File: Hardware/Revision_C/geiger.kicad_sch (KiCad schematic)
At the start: 23 parts, among them J1 I2C 5V, J2 I2C 3V3, J3 GND, U3 BSP125

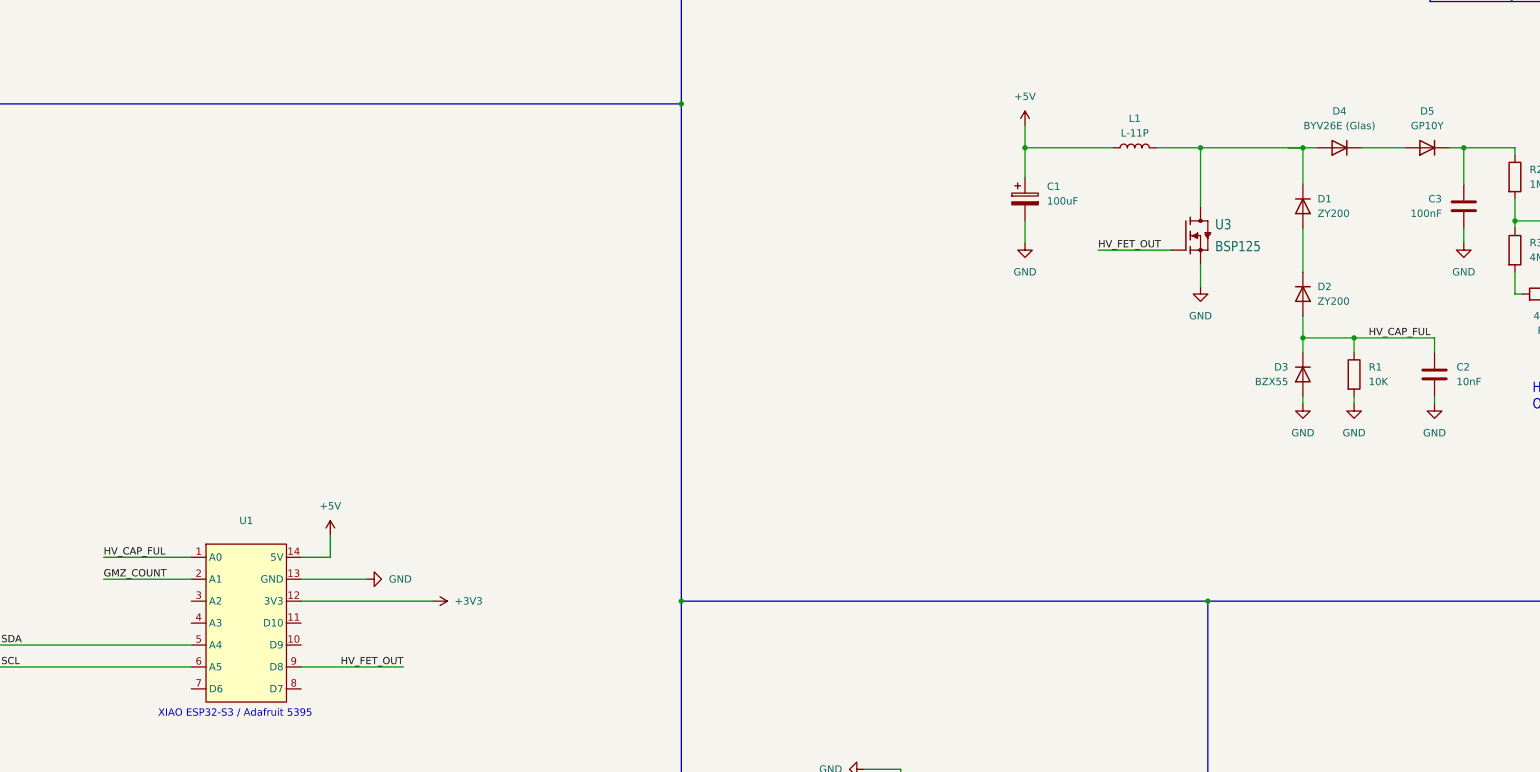
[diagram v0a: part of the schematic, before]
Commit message: Hardware: Rev B V2 + Rev C V2 — layout update to remove HV-to-counter crosstalk
Why these boards were redesigned:

The previous Rev B (Feather form factor) and Rev C (XIAO form factor)
carrier PCBs could register phantom Geiger counts: each pulse of the
high-voltage boost supply coupled a small spike into the tube counting
input. Long-term field data and bench probing traced the root cause to
the layout, not the circuit:

- The module socket pinout placed the counting input (GMZ_COUNT) directly
  beside the HV regulation sense net (HV_CAP_FUL), 2.54 mm pad to pad, so
  the most sensitive high-impedance node on the board (1 Mohm) was forced
  to run alongside its noisiest neighbour before routing even started.
- The counting trace crossed gaps in the ground plane (the worst void sat
  under the unused JP1 header on Rev B), weakening its return path exactly
  where the coupling occurred.

Firmware (V2.6.31+) fully compensates the phantom pulses by blanking, so
deployed nodes read correctly, but these V2 boards remove the coupling at
the source. What changed vs the previous revisions:

- Pin roles swapped at the module socket: GMZ_COUNT <-> HV_FET_OUT. The
  counting input now sits >=10 mm from both HV nets; the FET gate (a
  driven, low-impedance net) takes the seat next to the HV sense line.
- JP1 removed (Rev B), closing the ground-plane slot its through-holes cut.
- Routing rules enforced by DRC: >=2 mm clearance between the counting
  trace and both HV nets; crossings only on the opposite layer at 90 deg.
- Ground rebuilt: solid pours both sides with ~700 stitching vias; ground
  return coverage under the counting trace raised from ~79% to ~87%
  (Rev B; Rev C similar). The previous boards had no stitching vias near
  the counting run.
- Mounting holes enlarged 2.2 -> 2.7 mm to suit M2.5 hardware.
- The HV generation circuit itself is deliberately untouched: same
  schematic, same BOM, same tube chain.

IMPORTANT — FIRMWARE COMPATIBILITY: the pin-role swap makes b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
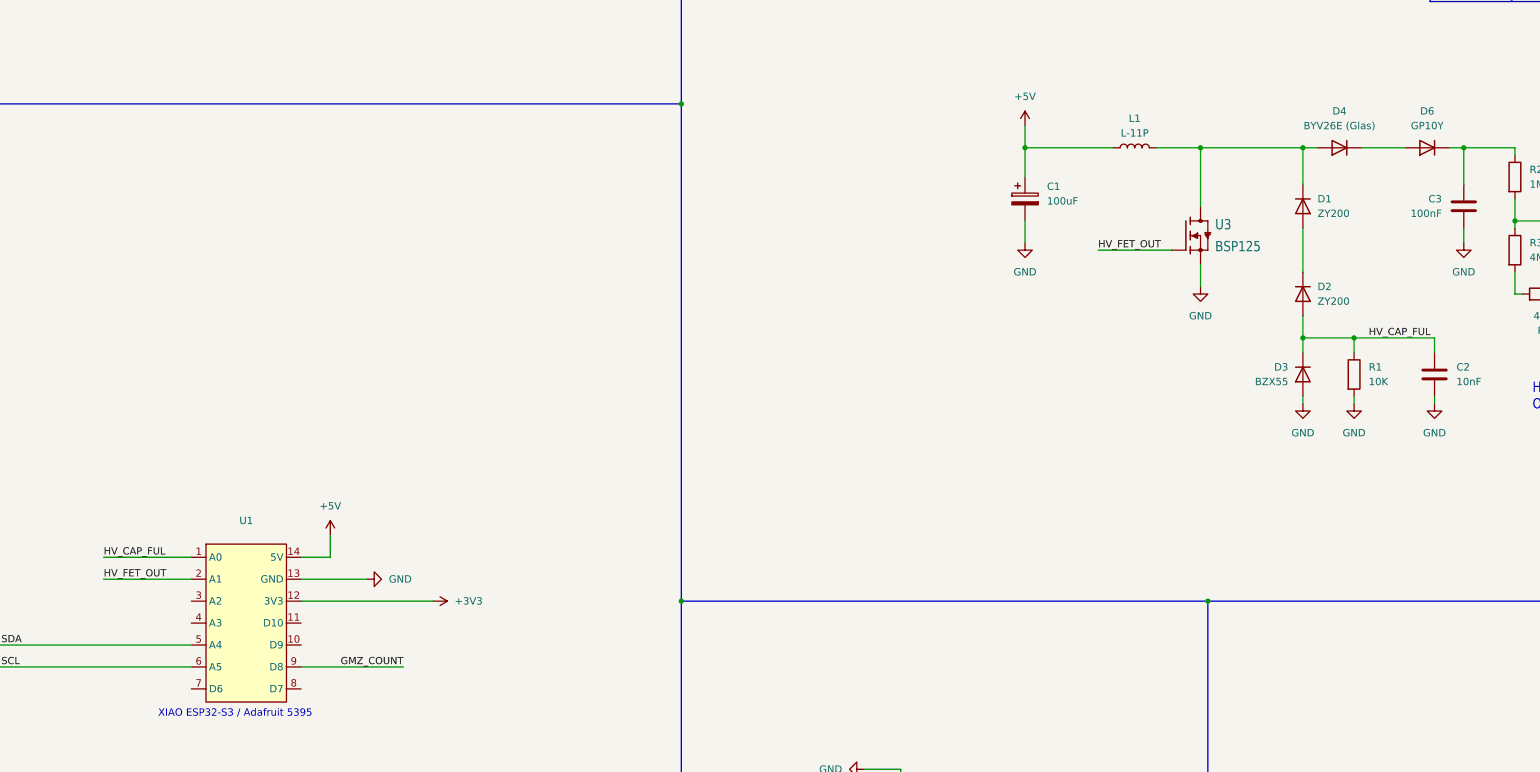
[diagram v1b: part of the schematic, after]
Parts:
- U1: value ~ -> (none)
- renumbered D5 to D6
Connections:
- net GMZ_COUNT: now also U1.9 (D8); no longer U1.2 (A1)
- net HV_FET_OUT: now also U1.2 (A1); no longer U1.9 (D8)

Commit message: Hardware: add manufacturer part numbers to the BOMs and schematics
Rev A: update PARTS in gen_v110_bom_cpl.py and regenerate the BOM.
Rev B and Rev C: add a Part Number field to each schematic symbol and
push it to the PCB footprints.

Part number updates: C3 R75 -> R76, D3 BZX55 -> BZX79-B3V3,
R2-R5 MFR-25 -> RNV14, R6 RNV14FAL100K.

Also fixes the D3 part number CSV quoting, adds the missing tube-clip
and GND test-point rows, corrects the D3 and L1 values, and renames the
Rev C tube holder to SBM-19/20 to match the PCB.

Board geometry is unchanged.
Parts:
- C1: Part Number (none) -> 16SEPC100MW
- C2: Part Number (none) -> MKP2D021001B00KSSD
- C3: Part Number (none) -> R76PI31005050J
- C4: Part Number (none) -> FKP2O101001D00JSSD
- D1, D2: Part Number (none) -> ZY200
- D3: value BZX55 -> BZX79-B3V3; Part Number (none) -> BZX79-B3V3,133
- D4: Part Number (none) -> BYV26E
- D6: Part Number (none) -> GP10Y
- J1: Part Number (none) -> PH-4P
- J2: Part Number (none) -> SM04B-SRSS-TB(LF)(SN)
- L1: value L-11P -> 150mH; Part Number (none) -> 11P-154J-50
- R1, R6, R7: Part Number (none) -> UXB02070F1002AR100
- R2, R5: Part Number (none) -> RNV14FAL1M00
- R3, R4: Part Number (none) -> RNV14FAL4M70
- SBM-19/20: renamed from SBM-19/1; Part Number (none) -> 8040.0003
- U3: Part Number (none) -> BSP125H6327
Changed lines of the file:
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@@
 		(dnp no)
 		(fields_autoplaced yes)
-		(property "Reference" "SBM-19/1"
+		(property "Reference" "SBM-19/20"
 			(at 382.27 95.2499 0)
 			(show_name no)
@@
 			)
 		)
-		(property "Untitled Field" ""
+		(property "Part Number" "8040.0003"
 			(at 383.8474 105.41 0)
 			(hide yes)
@@
 			(project "geiger"
 				(path "/29f38b98-cdf0-4588-b893-03ee7a6e5052"
-					(reference "SBM-19/1")
+					(reference "SBM-19/20")
 					(unit 1)
 				)
@@
 			)
 		)
-		(property "Untitled Field" ""
+		(property "Part Number" "RNV14FAL4M70"
 			(at 325.12 85.09 0)
 			(hide yes)
@@
 			)
 		)
-		(property "Untitled Field" ""
+		(property "Part Number" "16SEPC100MW"
 			(at 240.03 76.2 0)
 			(hide yes)
@@
 			)
 		)
-		(property "Value" "L-11P"
+		(property "Value" "150mH"
 			(at 259.08 64.77 90)
 			(show_name no)
@@
 			)
 		)
+		(property "Part Number" "11P-154J-50"
+			(at 259.08 67.31 90)
+			(hide yes)
+			(show_name no)
+			(do_not_autoplace no)
+			(effects
+				(font
+					(size 1.27 1.27)
+				)
+			)
+		)
 		(pin "2"
 		)
@@
 			)
 		)
-		(property "Untitled Field" ""
+		(property "Part Number" "RNV14FAL1M00"
 			(at 325.12 72.39 0)
 			(hide yes)
@@
 			)
 		)
+		(property "Part Number" "FKP2O101001D00JSSD"
+			(at 335.28 80.01 90)
+			(hide yes)
+			(show_name no)
+			(do_not_autoplace no)
+			(effects
+				(font
+					(size 1.27 1.27)
+				)
+			)
+		)
 		(pin "1"
 		)
@@
 			)
 		)
-		(property "Value" "BZX55"
+		(property "Value" "BZX79-B3V3"
 			(at 285.75 107.9499 90)
 			(show_name no)
@@
 			)
 		)
-		(property "Untitled Field" ""
-			(at 288.29 106.68 0)
+		(property "Part Number" "BZX79-B3V3,133"
+			(at 288.29 106.68 90)
 			(hide yes)
 			(show_name no)
@@
 			)
 		)
-		(property "Untitled Field" ""
-			(at 97.79 138.43 0)
-			(hide yes)
-			(show_name no)
-			(do_not_autoplace no)
-			(effects
-				(font
-					(size 1.27 1.27)
-				)
-			)
-		)
 		(pin "4"
 		)
@@
 			)
 		)
-		(property "Untitled Field" ""
-			(at 330.2 92.71 0)
+		(property "Part Number" "RNV14FAL4M70"
+			(at 330.2 92.71 90)
 			(hide yes)
 			(show_name no)
@@
 			)
 		)
-		(property "Untitled Field" ""
+		(property "Part Number" "BYV26E"
 			(at 294.64 67.31 0)
 			(hide yes)
@@
 			)
 		)
-		(property "Untitled Field" ""
+		(property "Part Number" "UXB02070F1002AR100"
 			(at 297.18 106.68 0)
 			(hide yes)
@@
 			)
 		)
+		(property "Part Number" "SM04B-SRSS-TB(LF)(SN)"
+			(at 218.44 187.96 0)
+			(hide yes)
+			(show_name no)
+			(do_not_autoplace no)
+			(effects
+				(font
+					(size 1.27 1.27)
+				)
+			)
+		)
 		(pin "3"
 		)
@@
 			)
 		)
-		(property "Untitled Field" ""
-			(at 55.88 153.67 0)
+		(property "Part Number" "UXB02070F1002AR100"
+			(at 55.88 153.67 90)
 			(hide yes)
 			(show_name no)
@@
 			)
 		)
-		(property "Untitled Field" ""
-			(at 288.29 92.71 0)
+		(property "Part Number" "ZY200"
+			(at 288.29 92.71 90)
 			(hide yes)
 			(show_name no)
@@
 			)
 		)
-		(property "Untitled Field" ""
-			(at 288.29 77.47 0)
+		(property "Part Number" "ZY200"
+			(at 288.29 77.47 90)
 			(hide yes)
 			(show_name no)
@@
 			)
 		)
-		(property "Untitled Field" ""
+		(property "Part Number" "GP10Y"
 			(at 309.88 67.31 0)
 			(hide yes)
@@
 			)
 		)
+		(property "Part Number" "MKP2D021001B00KSSD"
+			(at 311.15 106.68 0)
+			(hide yes)
+			(show_name no)
+			(do_not_autoplace no)
+			(effects
+				(font
+					(size 1.27 1.27)
+				)
+			)
+		)
 		(pin "1"
 		)
@@
 			)
 		)
+		(property "Part Number" "RNV14FAL1M00"
+			(at 342.9 72.39 0)
+			(hide yes)
+			(show_name no)
+			(do_not_autoplace no)
+			(effects
+				(font
+					(size 1.27 1.27)
+				)
+			)
+		)
 		(pin "2"
 		)
@@
 			)
 		)
+		(property "Part Number" "R76PI31005050J"
+			(at 316.23 77.47 0)
+			(hide yes)
+			(show_name no)
+			(do_not_autoplace no)
+			(effects
+				(font
+					(size 1.27 1.27)
+				)
+			)
+		)
 		(pin "1"
 		)
@@
 			)
 		)
-		(property "Untitled Field" ""
+		(property "Part Number" "BSP125H6327"
 			(at 267.97 82.55 0)
 			(hide yes)
@@
 			)
 		)
+		(property "Part Number" "PH-4P"
+			(at 288.29 200.66 0)
+			(hide yes)
+			(show_name no)
+			(do_not_autoplace no)
+			(effects
+				(font
+					(size 1.27 1.27)
+				)
+			)
+		)
 		(pin "3"
 		)
@@
 			)
 		)
-		(property "Untitled Field" ""
-			(at 55.88 157.48 0)
+		(property "Part Number" "UXB02070F1002AR100"
+			(at 55.88 157.48 90)
 			(hide yes)
 			(show_name no)
